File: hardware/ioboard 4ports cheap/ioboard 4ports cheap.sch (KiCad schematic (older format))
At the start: 38 parts, among them J1 Conn_02x06_Odd_Even, J2 Conn_01x03, J3 XLR3, J4 Conn_01x03, J5 XLR3, J6 Conn_01x03, J7 XLR3, J8 Conn_01x03, J9 XLR3, U1 M24C02-WMN, U2 SP3485EN, U3 SP3485EN, U4 SP3485EN, U5 SP3485EN

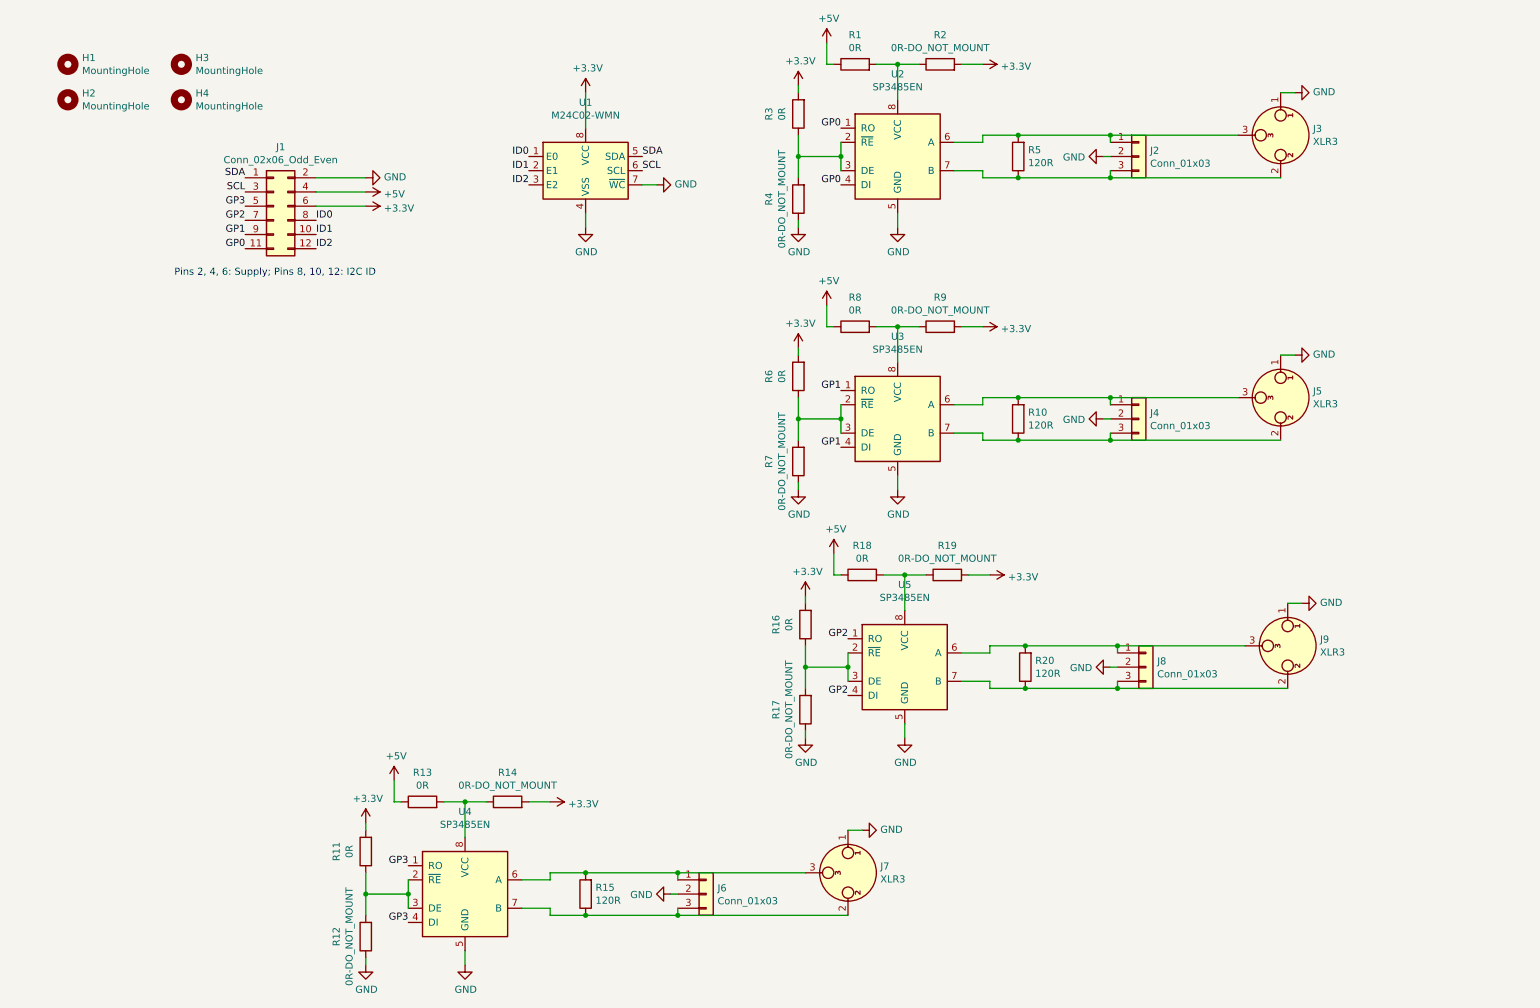
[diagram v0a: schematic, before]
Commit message: Re-work ioboard 4ports cheap. Should be production-ready
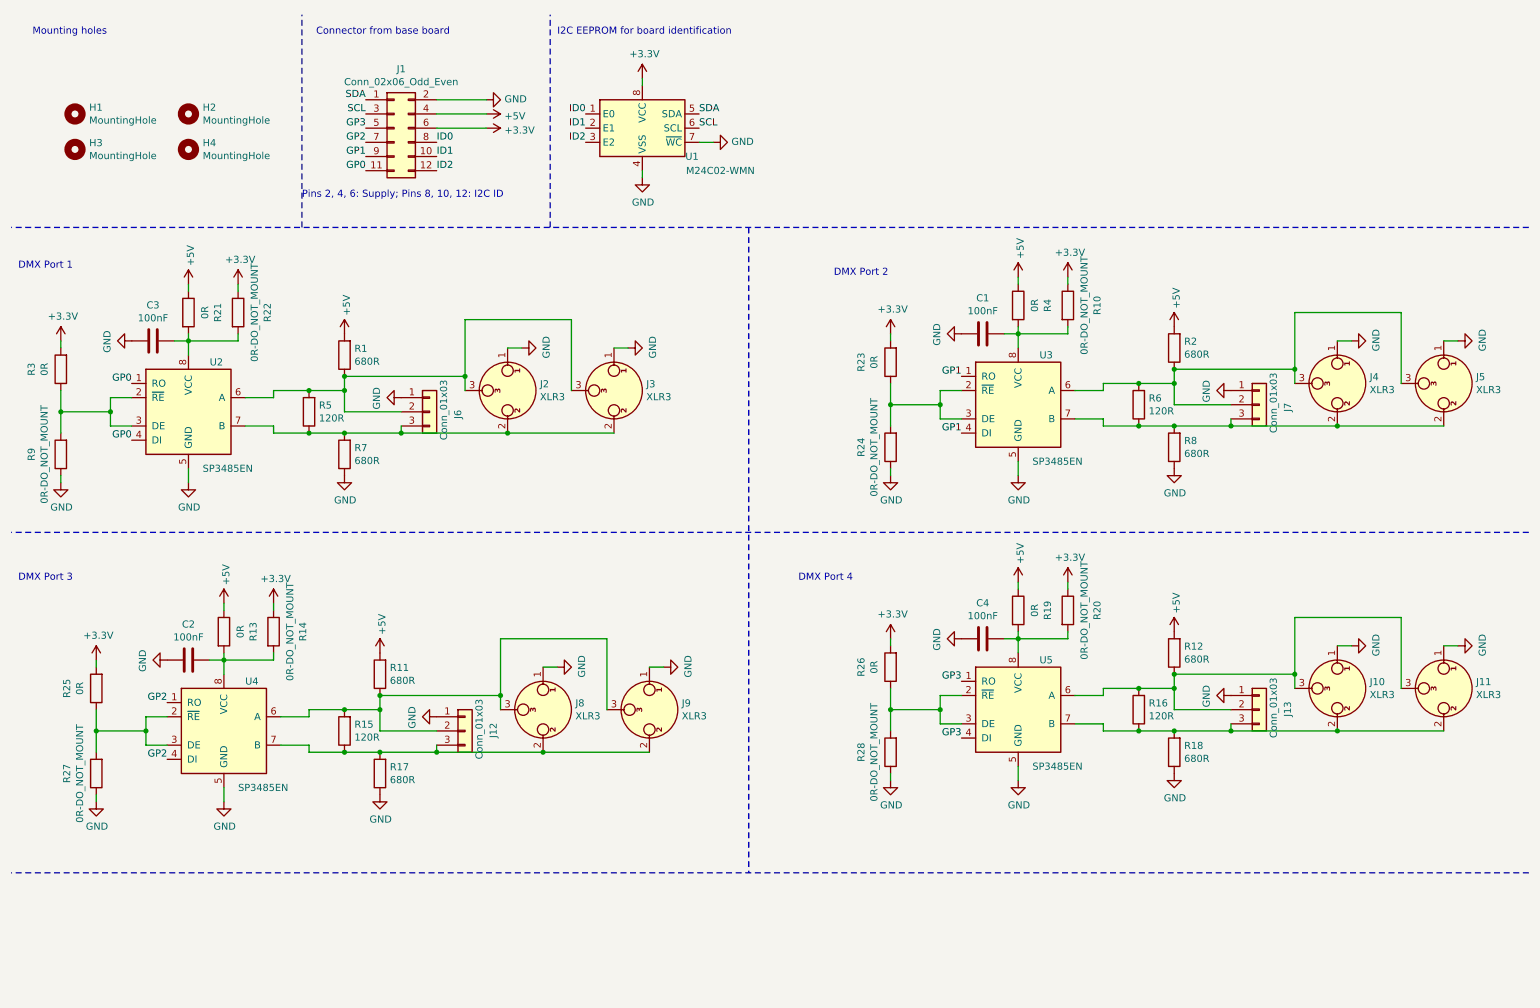
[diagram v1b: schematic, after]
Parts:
- removed J4, J6, J8: Conn_01x03, Connector_PinHeader_2.54mm:PinHeader_1x03_P2.54mm_Vertical, symbol Connector_Generic:Conn_01x03
- removed J7: XLR3, Connector_Audio:Jack_XLR_Neutrik_NC3FAAH_Horizontal, symbol Connector:XLR3
- removed R9: 0R-DO_NOT_MOUNT, Resistor_SMD:R_0603_1608Metric_Pad0.98x0.95mm_HandSolder, symbol Device:R
- added C1, C2, C3, C4: 100nF, Capacitor_SMD:C_0603_1608Metric, symbol Device:C
- added J10, J4, J8: XLR3, Connector_Audio:Jack_XLR_Neutrik_NC3FAAH_Horizontal, symbol Connector:XLR3
- added J11, J3: XLR3, NC3FD-H:Jack_XLR_Neutrik_NC3FD-H_Horizontal, symbol Connector:XLR3
- added J12, J13, J7: Conn_01x03, Connector_PinHeader_2.54mm:PinHeader_1x03_P2.54mm_Vertical, symbol Connector_Generic:Conn_01x03
- added R21, R23, R25, R26, R4: 0R, Resistor_SMD:R_0805_2012Metric_Pad1.20x1.40mm_HandSolder, symbol Device:R
- added R22, R24, R27, R28: 0R-DO_NOT_MOUNT, Resistor_SMD:R_0805_2012Metric_Pad1.20x1.40mm_HandSolder, symbol Device:R
- J5, J9: footprint Connector_Audio:Jack_XLR_Neutrik_NC3FAAH_Horizontal -> NC3FD-H:Jack_XLR_Neutrik_NC3FD-H_Horizontal
- R1, R11, R18, R8: value 0R -> 680R; LCSC (none) -> C23228
- R10, R20: value 120R -> 0R-DO_NOT_MOUNT; footprint Resistor_SMD:R_0603_1608Metric_Pad0.98x0.95mm_HandSolder -> Resistor_SMD:R_0805_2012Metric_Pad1.20x1.40mm_HandSolder; LCSC (none) -> C17477
- R12, R17, R2, R7: value 0R-DO_NOT_MOUNT -> 680R; LCSC (none) -> C23228
- R13, R14, R3: footprint Resistor_SMD:R_0603_1608Metric_Pad0.98x0.95mm_HandSolder -> Resistor_SMD:R_0805_2012Metric_Pad1.20x1.40mm_HandSolder; LCSC (none) -> C17477
- R15, R5: LCSC (none) -> C22787
- R16, R6: value 0R -> 120R; LCSC (none) -> C22787
- R19: value 0R-DO_NOT_MOUNT -> 0R; footprint Resistor_SMD:R_0603_1608Metric_Pad0.98x0.95mm_HandSolder -> Resistor_SMD:R_0805_2012Metric_Pad1.20x1.40mm_HandSolder; LCSC (none) -> C17477
- R9: renamed from R4; footprint Resistor_SMD:R_0603_1608Metric_Pad0.98x0.95mm_HandSolder -> Resistor_SMD:R_0805_2012Metric_Pad1.20x1.40mm_HandSolder; LCSC (none) -> C17477
- U1: LCSC (none) -> C7562
- U2, U3, U4, U5: LCSC (none) -> C8963
- renumbered H3 to H2, H2 to H3, J3 to J2, J2 to J6
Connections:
- net +3V3: now also R10.1, R14.1, R20.1, R22.1, R23.2, R25.2, R26.2; no longer R11.2, R14.2, R16.2, R19.2, R2.2, R6.2
- net +5V: now also R1.2, R11.2, R12.2, R19.1, R2.2, R21.1, R4.1; no longer R1.1, R18.1, R8.1
- net GND: now also J6.1 (Pin_1), R18.1, R8.1, C1.2, C2.2, C3.2, C4.2, J10.1, J11.1, J12.1 (Pin_1), J13.1 (Pin_1), J3.1, J4.1, J7.1 (Pin_1), J8.1, R24.1, R27.1, R28.1; no longer J6.2 (Pin_2), R12.1
- net GP2: now also U4.1 (RO), U4.4 (DI); no longer U5.1 (RO), U5.4 (DI)
- net GP3: now also U5.1 (RO), U5.4 (DI); no longer U4.1 (RO), U4.4 (DI)
- net at J2.3, R5.2, U2.6 (A): now also J6.2 (Pin_2), R1.1, J3.3; no longer J6.1 (Pin_1)
- net at J2.2, J6.3 (Pin_3), R5.1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: now also R7.2, J3.2
- net at U3.2 (~RE~), U3.3 (DE): now also R23.1, R24.2; no longer R6.1, R7.2
- net at J5.3, U3.6 (A): now also R2.1, R6.2, J4.3, J7.2 (Pin_2); no longer R10.2
- net at J5.2, U3.7 (B): now also R6.1, R8.2, J4.2, J7.3 (Pin_3); no longer R10.1
- net at U3.8 (VCC): now also R10.2, C1.1, R4.2; no longer R8.2
- net at U5.2 (~RE~), U5.3 (DE): now also R26.1, R28.2; no longer R16.1, R17.2
- net at U4.2 (~RE~), U4.3 (DE): now also R25.1, R27.2; no longer R11.1, R12.2
- net at R15.2, U4.6 (A): now also J9.3, R11.1, J12.2 (Pin_2), J8.3
- net at R15.1, U4.7 (B): now also J9.2, R17.2, J12.3 (Pin_3), J8.2
- net at R13.2, U4.8 (VCC): now also R14.2, C2.1; no longer R14.1
- new net: C3.1, R21.2, R22.2, U2.8 (VCC)
- new net: J10.2, J11.2, J13.3 (Pin_3), R16.1, R18.2, U5.7 (B)
- new net: J10.3, J11.3, J13.2 (Pin_2), R12.1, R16.2, U5.6 (A)
- new net: C4.1, R19.2, R20.2, U5.8 (VCC)
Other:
- note added: "Connector from base board"
- note added: "DMX Port 1"
- note added: "DMX Port 2"
- note added: "DMX Port 3"
- note added: "DMX Port 4"
- note added: "I2C EEPROM for board identification"
- note added: "Mounting holes"
- moved on the sheet: H1, H2, H3, H4, J1, J2, J6, R3, R5, R9, U1
